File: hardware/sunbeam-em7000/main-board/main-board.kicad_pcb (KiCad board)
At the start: 2 copper layers, 0 parts

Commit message: main-board: placement candidate 1
Co-Authored-By: Claude Sonnet 5.5 <noreply@anthropic.com>
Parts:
- added C101: 100nF_X2, Capacitor_THT:C_Rect_L13.0mm_W6.0mm_P10.00mm_FKS3_FKP3_MKS4, F.Cu at (14.5, 77.0)
- added C201: 100n, Capacitor_SMD:C_0603_1608Metric, F.Cu at (56.0, 109.0)
- added C202: 100n, Capacitor_SMD:C_1206_3216Metric, F.Cu at (59.0, 113.5)
- added C203: 4.7n, Capacitor_SMD:C_0603_1608Metric, F.Cu at (70.8, 112.2)
- added C204: 100n, Capacitor_SMD:C_1206_3216Metric, F.Cu at (62.7, 111.5)
- added C205: 4.7n, Capacitor_SMD:C_0603_1608Metric, F.Cu at (61.6, 106.3)
- added C301: 100 nF, Capacitor_SMD:C_0603_1608Metric, F.Cu at (87.0, 61.2)
- added C302: 47 uF, Capacitor_SMD:CP_Elec_6.3x5.2, F.Cu at (86.0, 67.8)
- added C303: 10 uF, Capacitor_SMD:C_0603_1608Metric, F.Cu at (83.3, 45.4)
- added C304: 22 uF, Capacitor_SMD:C_0805_2012Metric, F.Cu at (86.3, 37.3)
- added C305: 22 uF, Capacitor_SMD:C_0805_2012Metric, F.Cu at (85.2, 35.1)
- added C401: 100 nF, Capacitor_SMD:C_0603_1608Metric, F.Cu at (87.2, 28.9)
- added C402: 100 nF, Capacitor_SMD:C_0603_1608Metric, F.Cu at (102.2, 24.7)
- added C403: 100 nF, Capacitor_SMD:C_0603_1608Metric, F.Cu at (103.0, 11.9)
- added C404: 100 nF, Capacitor_SMD:C_0603_1608Metric, F.Cu at (85.8, 8.05)
- added C405: 100 nF, Capacitor_SMD:C_0603_1608Metric, F.Cu at (82.8, 25.2)
- added C406: 100 nF, Capacitor_SMD:C_0603_1608Metric, F.Cu at (85.5, 28.9)
- added C407: 4.7 uF, Capacitor_SMD:C_0603_1608Metric, F.Cu at (103.0, 10.2)
- added C408: 100 nF, Capacitor_SMD:C_0603_1608Metric, F.Cu at (99.7, 29.1)
- added C409: 1 uF, Capacitor_SMD:C_0603_1608Metric, F.Cu at (101.4, 29.1)
- added C410: 100 nF, Capacitor_SMD:C_0603_1608Metric, F.Cu at (96.3, 29.1)
- added C411: 1 uF, Capacitor_SMD:C_0603_1608Metric, F.Cu at (98.0, 29.1)
- added C412: 2.2 uF, Capacitor_SMD:C_0603_1608Metric, F.Cu at (103.0, 13.6)
- added C413: 2.2 uF, Capacitor_SMD:C_0603_1608Metric, F.Cu at (87.5, 8.05)
- added C414: 20 pF, Capacitor_SMD:C_0603_1608Metric, F.Cu at (89.0, 32.5)
- added C415: 20 pF, Capacitor_SMD:C_0603_1608Metric, F.Cu at (93.3, 34.6)
- added C416: 4.7 pF, Capacitor_SMD:C_0603_1608Metric, F.Cu at (83.8, 28.9)
- added C417: 4.7 pF, Capacitor_SMD:C_0603_1608Metric, F.Cu at (85.8, 31.4)
- added C418: 100 nF, Capacitor_SMD:C_0603_1608Metric, F.Cu at (114.3, 31.8)
- added C419: 4.7 nF, Capacitor_SMD:C_1206_3216Metric, F.Cu at (79.7, 7.65)
- added C422: 100 nF, Capacitor_SMD:C_0603_1608Metric, F.Cu at (101.1, 64.4)
- added C501: 47n, Capacitor_SMD:C_0603_1608Metric, F.Cu at (97.0, 31.5)
- added C502: 47n, Capacitor_SMD:C_0603_1608Metric, F.Cu at (103.8, 28.3)
- added C503: 47n, Capacitor_SMD:C_0603_1608Metric, F.Cu at (108.3, 20.7)
- added C520: 47n, Capacitor_SMD:C_0603_1608Metric, F.Cu at (123.5, 23.7)
- added C521: 100n, Capacitor_SMD:C_0603_1608Metric, F.Cu at (113.8, 17.6)
- added C522: 47n, Capacitor_SMD:C_0603_1608Metric, F.Cu at (105.8, 16.5)
- added C523: 47n, Capacitor_SMD:C_0603_1608Metric, F.Cu at (105.8, 21.6)
- added C524: 47n, Capacitor_SMD:C_0603_1608Metric, F.Cu at (106.3, 29.1)
- added C570: 47n, Capacitor_SMD:C_0603_1608Metric, F.Cu at (105.9, 32.5)
- added C571: 47n, Capacitor_SMD:C_0603_1608Metric, F.Cu at (107.5, 26.6)
- added C601: 4.7n, Capacitor_SMD:C_0805_2012Metric, F.Cu at (54.4, 88.3)
- added C602: 4.7n, Capacitor_SMD:C_0805_2012Metric, F.Cu at (54.4, 86.1)
- added C603: 1u, Capacitor_SMD:C_0603_1608Metric, F.Cu at (53.7, 78.2)
- added C604: 1n, Capacitor_SMD:C_0603_1608Metric, F.Cu at (55.4, 78.3)
- added C605: 100n, Capacitor_SMD:C_0603_1608Metric, F.Cu at (51.5, 83.3)
- added C606: 1n, Capacitor_SMD:C_0603_1608Metric, F.Cu at (52.0, 78.4)
- added C607: 100n, Capacitor_SMD:C_1206_3216Metric, F.Cu at (53.8, 81.2)
- added C608: 1n, Capacitor_SMD:C_0603_1608Metric, F.Cu at (54.6, 83.3)
- added C609: 1n, Capacitor_SMD:C_0603_1608Metric, F.Cu at (70.3, 85.3)
- added C610: 1u, Capacitor_SMD:C_0603_1608Metric, F.Cu at (69.6, 87.8)
- added C611: 100n, Capacitor_SMD:C_0603_1608Metric, F.Cu at (72.5, 91.2)
- added C612: 100n, Capacitor_SMD:C_0603_1608Metric, F.Cu at (69.6, 82.8)
- added C630: 1n, Capacitor_SMD:C_0603_1608Metric, F.Cu at (102.6, 96.5)
- added C640: 10n, Capacitor_SMD:C_0603_1608Metric, F.Cu at (82.7, 106.5)
- added C641: 100n, Capacitor_SMD:C_0603_1608Metric, F.Cu at (79.2, 100.0)
- added C642: 100n, Capacitor_SMD:C_0603_1608Metric, F.Cu at (79.2, 101.7)
- added C645: 10n, Capacitor_SMD:C_0603_1608Metric, F.Cu at (85.3, 116.5)
- added C646: 100n, Capacitor_SMD:C_0603_1608Metric, F.Cu at (80.2, 107.7)
- added C647: 100n, Capacitor_SMD:C_0603_1608Metric, F.Cu at (82.7, 108.5)
- added C670: 100n, Capacitor_SMD:C_0603_1608Metric, F.Cu at (89.3, 108.2)
- added C671: 10u, Capacitor_SMD:C_0805_2012Metric, F.Cu at (89.1, 100.5)
- added C672: 100n, Capacitor_SMD:C_0603_1608Metric, F.Cu at (98.7, 113.2)
- added C673: 100n, Capacitor_SMD:C_0603_1608Metric, F.Cu at (98.7, 100.2)
- added C675: 100n, Capacitor_SMD:C_0603_1608Metric, F.Cu at (89.3, 118.9)
- added C676: 10u, Capacitor_SMD:C_0805_2012Metric, F.Cu at (89.1, 111.7)
- added C677: 100n, Capacitor_SMD:C_0603_1608Metric, F.Cu at (95.1, 122.0)
- added C678: 100n, Capacitor_SMD:C_0603_1608Metric, F.Cu at (98.7, 110.0)
- added C701: 100nF_X2, Capacitor_THT:C_Rect_L13.0mm_W6.0mm_P10.00mm_FKS3_FKP3_MKS4, F.Cu at (41.5, 39.9)
- added C711: 100nF_X2, Capacitor_THT:C_Rect_L13.0mm_W6.0mm_P10.00mm_FKS3_FKP3_MKS4, F.Cu at (41.5, 10.9)
- added C791: 100n, Capacitor_SMD:C_0603_1608Metric, F.Cu at (87.1, 47.2)
- added C792: 47u, Capacitor_SMD:CP_Elec_5x5.4, F.Cu at (92.0, 49.0)
- added C861: 100n, Capacitor_SMD:C_0603_1608Metric, F.Cu at (110.2, 7.55)
- added C862: 100n, Capacitor_SMD:C_0603_1608Metric, F.Cu at (112.8, 8.35)
- added C863: 100n, Capacitor_SMD:C_0603_1608Metric, F.Cu at (122.1, 118.0)
- added D201: BAT54HT1G, Diode_SMD:D_SOD-323, F.Cu at (64.0, 115.2)
- added D202: BAS116, Package_TO_SOT_SMD:SOT-23, F.Cu at (69.2, 115.1)
- added D203: BAT54HT1G, Diode_SMD:D_SOD-323, F.Cu at (65.5, 112.2)
- added D204: BAS116, Package_TO_SOT_SMD:SOT-23, F.Cu at (66.5, 108.5)
- added D205: BAS116, Package_TO_SOT_SMD:SOT-23, F.Cu at (63.2, 97.7)
- added D206: BAS116, Package_TO_SOT_SMD:SOT-23, F.Cu at (66.9, 96.2)
- added D401: USBLC6-2SC6, Package_TO_SOT_SMD:SOT-23-6, F.Cu at (68.8, 8.20)
- added D402: SMF6.0A, Diode_SMD:D_SOD-123F, F.Cu at (82.8, 4.30)
- added D501: PESD5V0F1BL, Diode_SMD:D_SOD-882, F.Cu at (117.2, 39.5)
- added D502: BAT54S, Package_TO_SOT_SMD:SOT-23, F.Cu at (109.5, 17.2)
- added D503: PESD5V0F1BL, Diode_SMD:D_SOD-882, F.Cu at (117.4, 48.0)
- added D504: BAT54S, Package_TO_SOT_SMD:SOT-23, F.Cu at (110.7, 66.2)
- added D505: PESD5V0F1BL, Diode_SMD:D_SOD-882, F.Cu at (122.8, 55.5)
- added D506: BAT54S, Package_TO_SOT_SMD:SOT-23, F.Cu at (110.7, 111.9)
- added D520: PESD5V0F1BL, Diode_SMD:D_SOD-882, F.Cu at (122.9, 20.4)
- added D521: PESD5V0F1BL, Diode_SMD:D_SOD-882, F.Cu at (107.1, 125.8)
- added D522: PESD5V0F1BL, Diode_SMD:D_SOD-882, F.Cu at (109.6, 125.8)
- added D523: BAT54S, Package_TO_SOT_SMD:SOT-23, F.Cu at (102.0, 53.1)
- added D524: BAT54S, Package_TO_SOT_SMD:SOT-23, F.Cu at (101.8, 57.0)
- added D525: PESD5V0F1BL, Diode_SMD:D_SOD-882, F.Cu at (118.7, 120.2)
- added D526: PESD5V0F1BL, Diode_SMD:D_SOD-882, F.Cu at (121.1, 125.8)
- added D527: BAT54S, Package_TO_SOT_SMD:SOT-23, F.Cu at (120.4, 12.8)
- added D528: BAT54S, Package_TO_SOT_SMD:SOT-23, F.Cu at (102.0, 49.2)
- added D529: PESD5V0F1BL, Diode_SMD:D_SOD-882, F.Cu at (109.3, 52.3)
- added D530: PESD5V0F1BL, Diode_SMD:D_SOD-882, F.Cu at (122.8, 70.0)
- added D531: PESD5V0F1BL, Diode_SMD:D_SOD-882, F.Cu at (106.5, 66.6)
- added D570: PESD5V0F1BL, Diode_SMD:D_SOD-882, F.Cu at (113.6, 54.6)
- added D571: PESD5V0F1BL, Diode_SMD:D_SOD-882, F.Cu at (111.0, 54.6)
- added D731: 1N4148WS, Diode_SMD:D_SOD-323, F.Cu at (71.7, 45.6)
- added D741: 1N4148WS, Diode_SMD:D_SOD-323, F.Cu at (69.5, 46.5)
- added D821: 1N4148WS, Diode_SMD:D_SOD-323, F.Cu at (95.0, 42.6)
- added F101: 10A_T_250V, Fuse:Fuseholder_Clip-5x20mm_Bel_FC-203-22_Lateral_P17.80x5.00mm_D1.17mm_Horizontal, F.Cu at (38.0, 93.4)
- added F401: MF-MSMF050-2, Fuse:Fuse_1812_4532Metric, F.Cu at (79.2, 12.0)
- added F520: MF-NSMF012-2, Fuse:Fuse_1206_3216Metric, F.Cu at (103.0, 93.2)
- added F521: MF-NSMF012-2, Fuse:Fuse_1206_3216Metric, F.Cu at (104.4, 118.3)
- added F522: MF-NSMF012-2, Fuse:Fuse_1206_3216Metric, F.Cu at (123.2, 60.0)
- added F523: MF-NSMF012-2, Fuse:Fuse_1206_3216Metric, F.Cu at (109.8, 99.2)
- added F524: MF-NSMF012-2, Fuse:Fuse_1206_3216Metric, F.Cu at (115.5, 87.5)
- added F601: 600R@100MHz, Inductor_SMD:L_0603_1608Metric, F.Cu at (49.5, 77.7)
- added F602: 600R@100MHz, Inductor_SMD:L_0603_1608Metric, F.Cu at (47.8, 86.0)
- added F701: 0.8A, main-board:FUSEHOLDER_5x20_XC_BLX-A, F.Cu at (26.0, 31.4)
- added F711: 0.5A, main-board:FUSEHOLDER_5x20_XC_BLX-A, F.Cu at (26.0, 19.4)
- added F731: 0.4A, main-board:FUSEHOLDER_5x20_XC_BLX-A, F.Cu at (21.5, 66.0)
- added FB301: 600R@100MHz, Inductor_SMD:L_0603_1608Metric, F.Cu at (105.1, 25.9)
- added FID1: Fiducial, Fiducial_1mm_Mask2mm, F.Cu at (14.0, 5.50)
- added FID2: Fiducial, Fiducial_1mm_Mask2mm, F.Cu at (14.0, 123.5)
- added FID3: Fiducial, Fiducial_1mm_Mask2mm, F.Cu at (129.0, 117.6)
- added H1: MountingHole, MountingHole_3.1mm_Lid, F.Cu at (6.50, 122.5)
- added H2: MountingHole, MountingHole_3.1mm_Lid, F.Cu at (126.7, 122.5)
- added H3: MountingHole, MountingHole_3.1mm_Lid, F.Cu at (6.50, 5.50)
- added H4: MountingHole, MountingHole_3.1mm_Lid, F.Cu at (127.0, 5.50)
- added J101: TAB1_LINE1, main-board:Tab_BZXC_BTC-3-PCB634908T, F.Cu at (8.50, 108.5)
- added J102: TAB2_LINE_IN, main-board:Tab_BZXC_BTC-3-PCB634908T, F.Cu at (8.50, 99.7)
- added J103: TAB3_NEUTRAL_IN, main-board:Tab_BZXC_BTC-3-PCB634908T, F.Cu at (8.50, 90.9)
- added J106: TAB6_COFVALVE, main-board:Tab_BZXC_BTC-3-PCB634908T, F.Cu at (8.50, 49.9)
- added J107: TAB7_COFFPUMP, main-board:Tab_BZXC_BTC-3-PCB634908T, F.Cu at (8.50, 37.6)
- added J108: TAB8_STEAMPUMP, main-board:Tab_BZXC_BTC-3-PCB634908T, F.Cu at (8.50, 27.8)
- added J109: TAB9_HOTVALVE, main-board:Tab_BZXC_BTC-3-PCB634908T, F.Cu at (8.50, 19.5)
- added J110: WB_RET, main-board:Tab_BZXC_BTC-3-PCB634908T, F.Cu at (8.50, 82.4)
- added J401: SWD, Connector_PinHeader_1.27mm:PinHeader_2x05_P1.27mm_Vertical_SMD, F.Cu at (119.5, 28.5)
- added J402: USB_PANEL, Connector_PinHeader_2.54mm:PinHeader_1x05_P2.54mm_Vertical, F.Cu at (68.5, 4.50)
- added J501: TEMP_C, Connector_PinHeader_2.54mm:PinHeader_1x02_P2.54mm_Vertical, F.Cu at (120.0, 39.5)
- added J502: TEMP_S, Connector_PinHeader_2.54mm:PinHeader_1x02_P2.54mm_Vertical, F.Cu at (120.0, 47.5)
- added J503: TEMP_W, Connector_PinHeader_2.54mm:PinHeader_1x02_P2.54mm_Vertical, F.Cu at (120.0, 55.5)
- added J520: FLOW, Connector_PinHeader_2.54mm:PinHeader_1x03_P2.54mm_Vertical, F.Cu at (115.0, 20.5)
- added J521: STM_D, Connector_PinHeader_2.54mm:PinHeader_1x04_P2.54mm_Vertical, F.Cu at (102.0, 123.0)
- added J522: BREW_D, Connector_PinHeader_2.54mm:PinHeader_1x04_P2.54mm_Vertical, F.Cu at (113.5, 123.0)
- added J523: SPARE_A, Connector_PinHeader_2.54mm:PinHeader_1x04_P2.54mm_Vertical, F.Cu at (106.5, 44.7)
- added J524: BREW_A, Connector_PinHeader_2.54mm:PinHeader_1x04_P2.54mm_Vertical, F.Cu at (120.0, 62.2)
- added J525: SPARE_AN2_H, Connector_PinHeader_2.54mm:PinHeader_1x04_P2.54mm_Vertical, F.Cu at (106.5, 56.2)
- added J570: CURR1_H, Connector_PinHeader_2.54mm:PinHeader_1x03_P2.54mm_Vertical, F.Cu at (116.0, 57.5)
- added J571: CURR2_H, Connector_PinHeader_2.54mm:PinHeader_1x03_P2.54mm_Vertical, F.Cu at (111.0, 57.5)
- added J620: PT1_H, Connector_JST:JST_XH_B4B-XH-A_1x04_P2.50mm_Vertical, F.Cu at (110.5, 86.2)
- added J622: PT1_2W_P, Connector_PinHeader_2.54mm:PinHeader_1x02_P2.54mm_Vertical, F.Cu at (106.2, 99.2)
- added J623: PT1_23W_N, Connector_PinHeader_2.54mm:PinHeader_1x02_P2.54mm_Vertical, F.Cu at (106.2, 105.7)
- added J625: PT2_H, Connector_JST:JST_XH_B4B-XH-A_1x04_P2.50mm_Vertical, F.Cu at (110.5, 72.2)
- added J627: PT2_2W_P, Connector_PinHeader_2.54mm:PinHeader_1x02_P2.54mm_Vertical, F.Cu at (115.8, 67.2)
- added J628: PT2_23W_N, Connector_PinHeader_2.54mm:PinHeader_1x02_P2.54mm_Vertical, F.Cu at (122.8, 78.7)
- added J630: WT1_H, Connector_JST:JST_PH_B5B-PH-K_1x05_P2.00mm_Vertical, F.Cu at (114.5, 99.5)
- added J635: WT2_H, Connector_JST:JST_PH_B5B-PH-K_1x05_P2.00mm_Vertical, F.Cu at (118.5, 74.5)
- added J761: WB_LV10, Connector_PinHeader_2.54mm:PinHeader_1x10_P2.54mm_Vertical, F.Cu at (130.0, 60.5)
- added J791: SP2, Connector_JST:JST_PH_B9B-PH-K_1x09_P2.00mm_Vertical, F.Cu at (129.0, 12.5)
- added J821: CON2, Connector_JST:JST_PH_B9B-PH-K_1x09_P2.00mm_Vertical, F.Cu at (129.0, 34.5)
- added J861: KNOB, Connector_JST:JST_PH_B4B-PH-K_1x04_P2.00mm_Vertical, F.Cu at (110.0, 11.5)
- added J862: REED, main-board:REED_PADS_P20.00mm, F.Cu at (122.0, 91.5)
- added JP101: LINK_LIVE, main-board:JP101_WireLink_P10mm, F.Cu at (34.0, 84.5)
- added JP301: SEL_5V, Connector_PinHeader_2.54mm:PinHeader_1x03_P2.54mm_Vertical, F.Cu at (90.0, 54.5)
- added JP302: LINK_3V3, Connector_PinHeader_2.54mm:PinHeader_1x02_P2.54mm_Vertical, F.Cu at (73.5, 35.7)
- added JP303: LINK_MOD, main-board:JP101_WireLink_P10mm, F.Cu at (26.5, 50.5)
- added JP401: BOOT0_HI, Connector_PinHeader_2.54mm:PinHeader_1x02_P2.54mm_Vertical, F.Cu at (66.2, 15.0)
- added JP402: LINK_VTREF, Connector_PinHeader_2.54mm:PinHeader_1x02_P2.54mm_Vertical, F.Cu at (66.2, 21.0)
- added JP761: LINK, Connector_PinHeader_2.54mm:PinHeader_1x02_P2.54mm_Vertical, F.Cu at (127.3, 55.9)
- added JP791: LINK, Connector_PinHeader_2.54mm:PinHeader_1x02_P2.54mm_Vertical, F.Cu at (98.0, 50.7)
- added JP821: LINK, Connector_PinHeader_2.54mm:PinHeader_1x02_P2.54mm_Vertical, F.Cu at (98.0, 57.2)
- added K201: HF115F-Q/005-1H, main-board:Relay_HF115F-Q_1H_Vertical, F.Cu at (55.5, 105.7)
- added K731: HF32FA-G/005-HSL1, main-board:RELAY_HF32FA-G_1H_TYPE1_THT, F.Cu at (60.7, 46.5)
- added K741: HF32FA-G/005-HSL1, main-board:RELAY_HF32FA-G_1H_TYPE1_THT, F.Cu at (60.7, 11.3)
- added Q201: NX3008NBK, Package_TO_SOT_SMD:SOT-23, F.Cu at (71.0, 107.6)
- added Q202: NX3008NBK, Package_TO_SOT_SMD:SOT-23, F.Cu at (67.3, 104.4)
- added Q701: AO3400A, Package_TO_SOT_SMD:SOT-23, F.Cu at (62.0, 25.8)
- added Q711: AO3400A, Package_TO_SOT_SMD:SOT-23, F.Cu at (64.5, 43.0)
- added Q731: AO3400A, Package_TO_SOT_SMD:SOT-23, F.Cu at (69.8, 35.5)
- added Q741: AO3400A, Package_TO_SOT_SMD:SOT-23, F.Cu at (68.5, 43.0)
- added Q761: AO3400A, Package_TO_SOT_SMD:SOT-23, F.Cu at (97.0, 76.3)
- added Q771: AO3400A, Package_TO_SOT_SMD:SOT-23, F.Cu at (94.0, 59.2)
- added Q821: AO3400A, Package_TO_SOT_SMD:SOT-23, F.Cu at (97.7, 69.5)
- added Q822: AO3401A, Package_TO_SOT_SMD:SOT-23, F.Cu at (98.0, 63.7)
- added Q823: AO3400A, Package_TO_SOT_SMD:SOT-23, F.Cu at (80.5, 45.5)
- added Q824: AO3400A, Package_TO_SOT_SMD:SOT-23, F.Cu at (73.5, 42.0)
- added R101: 1Meg, Resistor_SMD:R_1206_3216Metric, F.Cu at (26.4, 67.4)
- added R102: 1Meg, Resistor_SMD:R_1206_3216Metric, F.Cu at (27.9, 63.8)
- added R103: 1Meg, Resistor_SMD:R_1206_3216Metric, F.Cu at (19.1, 69.6)
- added R104: 1Meg, Resistor_SMD:R_1206_3216Metric, F.Cu at (19.1, 74.4)
- added R105: 1m, main-board:R_WSK2512_4T, F.Cu at (9.00, 86.7)
- added R201: 100k, Resistor_SMD:R_0603_1608Metric, F.Cu at (51.0, 112.2)
- added R202: 100k, Resistor_SMD:R_0603_1608Metric, F.Cu at (51.0, 110.5)
- added R203: 5.6Meg, Resistor_SMD:R_0603_1608Metric, F.Cu at (70.8, 110.5)
- added R204: 5.6Meg, Resistor_SMD:R_0603_1608Metric, F.Cu at (63.5, 104.6)
- added R205: 100k, Resistor_SMD:R_0603_1608Metric, F.Cu at (66.5, 116.0)
- added R206: 100k, Resistor_SMD:R_0603_1608Metric, F.Cu at (63.1, 108.2)
- added R207: 1k, Resistor_SMD:R_0603_1608Metric, F.Cu at (53.5, 110.1)
- added R301: 0, Resistor_SMD:R_0603_1608Metric, F.Cu at (117.2, 35.5)
- added R302: 0, Resistor_SMD:R_0603_1608Metric, F.Cu at (110.0, 20.7)
- added R401: 10k, Resistor_SMD:R_0603_1608Metric, F.Cu at (69.7, 12.2)
- added R402: 1k, Resistor_SMD:R_0603_1608Metric, F.Cu at (117.0, 23.9)
- added R403: 1Meg, Resistor_SMD:R_1206_3216Metric, F.Cu at (65.3, 5.75)
- added R501: 10k, Resistor_SMD:R_0603_1608Metric, F.Cu at (119.7, 36.8)
- added R502: 1k, Resistor_SMD:R_0603_1608Metric, F.Cu at (100.2, 31.5)
- added R503: 10k, Resistor_SMD:R_0603_1608Metric, F.Cu at (115.8, 48.0)
- added R504: 1k, Resistor_SMD:R_0603_1608Metric, F.Cu at (103.5, 31.7)
- added R505: 10k, Resistor_SMD:R_0603_1608Metric, F.Cu at (116.3, 50.5)
- added R506: 1k, Resistor_SMD:R_0603_1608Metric, F.Cu at (105.8, 19.9)
- added R520: 10k, Resistor_SMD:R_0603_1608Metric, F.Cu at (113.8, 23.3)
- added R521: 1k, Resistor_SMD:R_0603_1608Metric, F.Cu at (123.5, 22.0)
- added R522: 0, Resistor_SMD:R_0603_1608Metric, F.Cu at (95.0, 7.10)
- added R523: 100, Resistor_SMD:R_0603_1608Metric, F.Cu at (82.0, 22.6)
- added R524: 100, Resistor_SMD:R_0603_1608Metric, F.Cu at (81.1, 25.1)
- added R525: 2.2k, Resistor_SMD:R_0603_1608Metric, F.Cu at (69.7, 18.2)
- added R526: 2.2k, Resistor_SMD:R_0603_1608Metric, F.Cu at (66.5, 23.8)
- added R527: 100, Resistor_SMD:R_0603_1608Metric, F.Cu at (102.2, 16.1)
- added R528: 100, Resistor_SMD:R_0603_1608Metric, F.Cu at (105.4, 13.4)
- added R529: 2.2k, Resistor_SMD:R_0603_1608Metric, F.Cu at (113.5, 15.8)
- added R530: 2.2k, Resistor_SMD:R_0603_1608Metric, F.Cu at (105.4, 10.2)
- added R531: 10k, Resistor_SMD:R_0603_1608Metric, F.Cu at (110.0, 44.0)
- added R532: 20k, Resistor_SMD:R_0603_1608Metric, F.Cu at (105.9, 41.2)
- added R533: 1k, Resistor_SMD:R_0603_1608Metric, F.Cu at (105.8, 18.2)
- added R534: 10k, Resistor_SMD:R_0603_1608Metric, F.Cu at (124.6, 56.0)
- added R535: 20k, Resistor_SMD:R_0603_1608Metric, F.Cu at (124.3, 48.0)
- added R536: 1k, Resistor_SMD:R_0603_1608Metric, F.Cu at (105.8, 23.3)
- added R537: 10k, Resistor_SMD:R_0603_1608Metric, F.Cu at (111.0, 52.1)
- added R538: 20k, Resistor_SMD:R_0603_1608Metric, F.Cu at (110.2, 49.6)
- added R539: 1k, Resistor_SMD:R_0603_1608Metric, F.Cu at (103.8, 30.0)
- added R540: 0, Resistor_SMD:R_1206_3216Metric, F.Cu at (101.9, 111.8)
- added R541: 0, Resistor_SMD:R_1206_3216Metric, F.Cu at (112.6, 119.8)
- added R542: 0, Resistor_SMD:R_1206_3216Metric, F.Cu at (123.2, 52.0)
- added R543: 0, Resistor_SMD:R_1206_3216Metric, F.Cu at (114.8, 92.2)
- added R544: 0, Resistor_SMD:R_1206_3216Metric, F.Cu at (123.2, 66.8)
- added R570: 10k, Resistor_SMD:R_0603_1608Metric, F.Cu at (113.5, 50.5)
- added R571: 20k, Resistor_SMD:R_0603_1608Metric, F.Cu at (114.2, 46.5)
- added R572: DNP, Resistor_SMD:R_0603_1608Metric, F.Cu at (114.0, 43.4)
- added R573: 1k, Resistor_SMD:R_0603_1608Metric, F.Cu at (105.1, 35.6)
- added R574: 10k, Resistor_SMD:R_0603_1608Metric, F.Cu at (122.8, 41.8)
- added R575: 20k, Resistor_SMD:R_0603_1608Metric, F.Cu at (122.8, 36.9)
- added R576: DNP, Resistor_SMD:R_0603_1608Metric, F.Cu at (123.5, 39.4)
- added R577: 1k, Resistor_SMD:R_0603_1608Metric, F.Cu at (108.8, 28.3)
- added R601: 300k, Resistor_SMD:R_2512_6332Metric, F.Cu at (24.9, 72.6)
- added R602: 300k, Resistor_SMD:R_2512_6332Metric, F.Cu at (27.4, 78.6)
- added R603: 300k, Resistor_SMD:R_2512_6332Metric, F.Cu at (35.4, 80.3)
- added R604: 750, Resistor_SMD:R_0603_1608Metric, F.Cu at (45.5, 90.2)
- added R605: 49.9, Resistor_SMD:R_0603_1608Metric, F.Cu at (48.0, 89.5)
- added R606: 49.9, Resistor_SMD:R_0603_1608Metric, F.Cu at (48.0, 91.2)
- added R607: 330, Resistor_SMD:R_0603_1608Metric, F.Cu at (48.4, 87.8)
- added R608: 330, Resistor_SMD:R_0603_1608Metric, F.Cu at (51.0, 86.0)
- added R609: 33, Resistor_SMD:R_0603_1608Metric, F.Cu at (71.4, 82.9)
- added R610: 33, Resistor_SMD:R_0603_1608Metric, F.Cu at (101.4, 8.45)
- added R611: 33, Resistor_SMD:R_0603_1608Metric, F.Cu at (98.1, 8.80)
- added R612: 33, Resistor_SMD:R_0603_1608Metric, F.Cu at (98.2, 7.10)
- added R613: 33, Resistor_SMD:R_0603_1608Metric, F.Cu at (68.5, 90.5)
- added R614: 100k, Resistor_SMD:R_0603_1608Metric, F.Cu at (65.2, 90.5)
- added R615: 100k, Resistor_SMD:R_0603_1608Metric, F.Cu at (115.5, 35.6)
- added R630: 60.4k, Resistor_SMD:R_2512_6332Metric, F.Cu at (40.6, 121.8)
- added R631: 60.4k, Resistor_SMD:R_2512_6332Metric, F.Cu at (48.5, 122.7)
- added R632: 22k, Resistor_SMD:R_0603_1608Metric, F.Cu at (101.7, 104.0)
- added R640: 4.02k, Resistor_SMD:R_0603_1608Metric, F.Cu at (105.7, 86.1)
- added R641: 100k, Resistor_SMD:R_0603_1608Metric, F.Cu at (105.2, 89.3)
- added R642: 0, Resistor_SMD:R_0603_1608Metric, F.Cu at (79.5, 119.3)
- added R643: 0, Resistor_SMD:R_0603_1608Metric, F.Cu at (80.0, 104.2)
- added R645: 4.02k, Resistor_SMD:R_0603_1608Metric, F.Cu at (81.3, 120.8)
- added R646: 100k, Resistor_SMD:R_0603_1608Metric, F.Cu at (105.2, 92.5)
- added R647: 0, Resistor_SMD:R_0603_1608Metric, F.Cu at (83.8, 124.8)
- added R648: 0, Resistor_SMD:R_0603_1608Metric, F.Cu at (81.3, 124.0)
- added R670: 100, Resistor_SMD:R_0603_1608Metric, F.Cu at (98.7, 106.8)
- added R671: 100, Resistor_SMD:R_0603_1608Metric, F.Cu at (89.3, 105.0)
- added R672: 100k, Resistor_SMD:R_0603_1608Metric, F.Cu at (105.2, 95.8)
- added R675: 100, Resistor_SMD:R_0603_1608Metric, F.Cu at (89.2, 121.3)
- added R676: 100, Resistor_SMD:R_0603_1608Metric, F.Cu at (89.3, 115.7)
- added R677: 100k, Resistor_SMD:R_0603_1608Metric, F.Cu at (105.8, 115.6)
- added R690: 0, Resistor_SMD:R_0603_1608Metric, F.Cu at (105.2, 111.8)
- added R691: 0, Resistor_SMD:R_0603_1608Metric, F.Cu at (105.5, 82.9)
- added R701: 100, Resistor_SMD:R_0603_1608Metric, F.Cu at (89.2, 8.05)
- added R702: 100k, Resistor_SMD:R_0603_1608Metric, F.Cu at (69.0, 39.2)
- added R703: 180, Resistor_SMD:R_1206_3216Metric, F.Cu at (66.0, 46.0)
- added R704: 200, Resistor_SMD:R_1206_3216Metric, F.Cu at (45.0, 26.6)
- added R705: 200, Resistor_SMD:R_1206_3216Metric, F.Cu at (49.9, 26.6)
- added R706: 100, Resistor_SMD:R_2512_6332Metric, F.Cu at (34.8, 28.0)
- added R711: 100, Resistor_SMD:R_0603_1608Metric, F.Cu at (91.7, 7.10)
- added R712: 100k, Resistor_SMD:R_0603_1608Metric, F.Cu at (59.1, 26.0)
- added R713: 180, Resistor_SMD:R_1206_3216Metric, F.Cu at (77.8, 34.7)
- added R714: 200, Resistor_SMD:R_1206_3216Metric, F.Cu at (47.1, 14.5)
- added R715: 200, Resistor_SMD:R_1206_3216Metric, F.Cu at (52.0, 14.3)
- added R716: 100, Resistor_SMD:R_2512_6332Metric, F.Cu at (34.8, 22.7)
- added R731: 100, Resistor_SMD:R_0603_1608Metric, F.Cu at (81.1, 17.9)
- added R732: 100k, Resistor_SMD:R_0603_1608Metric, F.Cu at (83.3, 74.2)
- added R741: 100, Resistor_SMD:R_0603_1608Metric, F.Cu at (79.4, 18.0)
- added R742: 100k, Resistor_SMD:R_0603_1608Metric, F.Cu at (61.6, 36.5)
- added R761: 100, Resistor_SMD:R_0603_1608Metric, F.Cu at (82.8, 13.7)
- added R762: 100k, Resistor_SMD:R_0603_1608Metric, F.Cu at (93.6, 77.2)
- added R763: 180, Resistor_SMD:R_1206_3216Metric, F.Cu at (97.7, 73.0)
- added R764: 27k, Resistor_SMD:R_0603_1608Metric, F.Cu at (102.2, 19.2)
- added R765: 82k, Resistor_SMD:R_0603_1608Metric, F.Cu at (118.5, 7.55)
- added R771: 100, Resistor_SMD:R_0603_1608Metric, F.Cu at (82.8, 16.9)
- added R772: 100k, Resistor_SMD:R_0603_1608Metric, F.Cu at (95.6, 45.1)
- added R773: 180, Resistor_SMD:R_1206_3216Metric, F.Cu at (126.8, 64.0)
- added R774: 27k, Resistor_SMD:R_0603_1608Metric, F.Cu at (82.8, 20.1)
- added R775: 82k, Resistor_SMD:R_0603_1608Metric, F.Cu at (66.5, 18.2)
- added R791: 100, Resistor_SMD:R_0603_1608Metric, F.Cu at (84.7, 47.8)
- added R792: 100, Resistor_SMD:R_0603_1608Metric, F.Cu at (86.3, 49.8)
- added R793: 100, Resistor_SMD:R_0603_1608Metric, F.Cu at (85.2, 45.4)
- added R794: 100, Resistor_SMD:R_0603_1608Metric, F.Cu at (81.8, 35.4)
- added R795: 100, Resistor_SMD:R_0603_1608Metric, F.Cu at (92.4, 37.5)
- added R796: 1k, Resistor_SMD:R_0603_1608Metric, F.Cu at (80.3, 20.4)
- added R797: 1k, Resistor_SMD:R_0603_1608Metric, F.Cu at (94.9, 8.80)
- added R798: 1k, Resistor_SMD:R_0603_1608Metric, F.Cu at (84.2, 8.05)
- added R799: 1k, Resistor_SMD:R_0603_1608Metric, F.Cu at (91.7, 8.80)
- added R800: 1k, Resistor_SMD:R_0603_1608Metric, F.Cu at (75.7, 7.95)
- added R801: 10k, Resistor_SMD:R_0603_1608Metric, F.Cu at (93.7, 56.5)
- added R802: 10k, Resistor_SMD:R_0603_1608Metric, F.Cu at (90.8, 63.0)
- added R803: 10k, Resistor_SMD:R_0603_1608Metric, F.Cu at (87.2, 55.4)
- added R804: 10k, Resistor_SMD:R_0603_1608Metric, F.Cu at (87.1, 52.2)
- added R805: 10k, Resistor_SMD:R_0603_1608Metric, F.Cu at (76.8, 44.8)
- added R806: 10k, Resistor_SMD:R_0603_1608Metric, F.Cu at (83.8, 50.2)
- added R821: 100, Resistor_SMD:R_0603_1608Metric, F.Cu at (79.4, 22.9)
- added R822: 100k, Resistor_SMD:R_0603_1608Metric, F.Cu at (94.2, 70.5)
- added R823: 22k, Resistor_SMD:R_0603_1608Metric, F.Cu at (94.2, 68.6)
- added R824: 22k, Resistor_SMD:R_0603_1608Metric, F.Cu at (98.3, 66.6)
- added R825: 22k, Resistor_SMD:R_0603_1608Metric, F.Cu at (127.2, 59.4)
- added R826: 100, Resistor_SMD:R_0603_1608Metric, F.Cu at (80.0, 29.3)
- added R827: 100k, Resistor_SMD:R_0603_1608Metric, F.Cu at (62.5, 14.8)
- added R828: 100, Resistor_SMD:R_1206_3216Metric, F.Cu at (93.3, 66.5)
- added R829: 100, Resistor_SMD:R_0603_1608Metric, F.Cu at (79.4, 26.1)
- added R830: 100k, Resistor_SMD:R_0603_1608Metric, F.Cu at (74.2, 45.5)
- added R831: 10k, Resistor_SMD:R_0603_1608Metric, F.Cu at (79.3, 31.8)
- added R832: 10k, Resistor_SMD:R_0603_1608Metric, F.Cu at (69.7, 24.8)
- added R833: 10k, Resistor_SMD:R_0603_1608Metric, F.Cu at (82.0, 28.6)
- added R834: 10k, Resistor_SMD:R_0603_1608Metric, F.Cu at (82.6, 31.4)
- added R835: 10k, Resistor_SMD:R_0603_1608Metric, F.Cu at (69.7, 26.5)
- added R861: 10k, Resistor_SMD:R_0603_1608Metric, F.Cu at (108.5, 7.55)
- added R862: 10k, Resistor_SMD:R_0603_1608Metric, F.Cu at (116.0, 8.35)
- added R863: 10k, Resistor_SMD:R_0603_1608Metric, F.Cu at (119.6, 117.3)
- added RT301: NTC 10D-9, Capacitor_THT:C_Disc_D11.0mm_W5.0mm_P7.50mm, F.Cu at (15.3, 45.3)
- added RV101: 14D471K, Varistor:RV_Disc_D15.5mm_W5mm_P7.5mm, F.Cu at (19.5, 82.4)
- added SW401: RESET, main-board:TS1187A_5.1x5.1mm_SMD, F.Cu at (68.5, 30.5)
- added T701: BTA204S-600B, Package_TO_SOT_SMD:TO-252-3_TabPin2, F.Cu at (43.6, 31.4)
- added T711: BTA204S-600B, Package_TO_SOT_SMD:TO-252-3_TabPin2, F.Cu at (43.6, 19.4)
- added TP101: TP_LINE_IN, TestPoint:TestPoint_Pad_D1.5mm, B.Cu at (8.50, 103.8)
- added TP102: TP_LINE_F, TestPoint:TestPoint_Pad_D1.5mm, B.Cu at (13.0, 95.0)
- added TP103: TP_LINE, TestPoint:TestPoint_Pad_D1.5mm, B.Cu at (35.0, 121.8)
- added TP104: TP_LINE1, TestPoint:TestPoint_Pad_D1.5mm, B.Cu at (13.3, 104.2)
- added TP105: TP_NEUTRAL_IN, TestPoint:TestPoint_Pad_D1.5mm, B.Cu at (6.00, 95.0)
- added TP106: TP_NEUTRAL, TestPoint:TestPoint_Pad_D1.5mm, B.Cu at (25.5, 59.5)
- added TP107: TP_NEUTRAL_IN_V, TestPoint:TestPoint_Pad_D1.5mm, B.Cu at (9.00, 95.0)
- added TP108: TP_NEUTRAL_V, TestPoint:TestPoint_Pad_D1.5mm, B.Cu at (26.5, 57.0)
- added TP201: TP_POL_GATE_A, TestPoint:TestPoint_Pad_D1.5mm, B.Cu at (71.0, 103.8)
- added TP202: TP_POL_GATE_B, TestPoint:TestPoint_Pad_D1.5mm, B.Cu at (71.0, 101.0)
- added TP203: TP_POL_OUT, TestPoint:TestPoint_Pad_D1.5mm, B.Cu at (104.5, 3.95)
- added TP204: TP_POL_BUF, TestPoint:TestPoint_Pad_D1.5mm, B.Cu at (54.8, 114.0)
- added TP205: TP_POL_COIL_LO, TestPoint:TestPoint_Pad_D1.5mm, B.Cu at (59.0, 98.5)
- added TP206: TP_+5V, TestPoint:TestPoint_Pad_D1.5mm, B.Cu at (59.5, 110.5)
- added TP301: TP, TestPoint:TestPoint_Pad_D1.5mm, B.Cu at (86.0, 74.5)
- added TP302: TP, TestPoint:TestPoint_Pad_D1.5mm, B.Cu at (66.5, 39.5)
- added TP303: TP, TestPoint:TestPoint_Pad_D1.5mm, B.Cu at (84.5, 54.0)
- added TP401: TP, TestPoint:TestPoint_Pad_D1.5mm, B.Cu at (107.0, 3.95)
- added TP402: TP, TestPoint:TestPoint_Pad_D1.5mm, B.Cu at (108.5, 34.0)
- added TP403: TP, TestPoint:TestPoint_Pad_D1.5mm, B.Cu at (112.0, 4.00)
- added TP404: TP, TestPoint:TestPoint_Pad_D1.5mm, B.Cu at (65.5, 35.0)
- added TP405: TP, TestPoint:TestPoint_Pad_D1.5mm, B.Cu at (120.5, 16.5)
- added TP406: TP, TestPoint:TestPoint_Pad_D1.5mm, B.Cu at (95.8, 37.2)
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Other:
- board outline added: 131 x 125 mm
- copper layers 2 -> 4

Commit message: main-board: placement candidate 2
Co-Authored-By: Claude Sonnet 5.5 <noreply@anthropic.com>
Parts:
- moved R632 83.8 mm to (68.8, 26.9), turned to 0 degrees
- moved C630 79.1 mm to (66.3, 26.1), turned to 90 degrees
- moved D506 76.4 mm to (116.8, 35.8)
- moved R615 54.7 mm to (105.1, 89.3)
- moved R403 54.7 mm to (120.0, 6.95), turned to 0 degrees
- moved D502 49.0 mm to (110.7, 66.2)
- moved D504 45.7 mm to (110.2, 111.9)
- moved R827 41.1 mm to (83.2, 50.2), turned to -90 degrees
- moved TP409 41.0 mm to (113.3, 28.3)
- moved TP530 39.4 mm to (123.0, 73.5)
- moved R835 37.9 mm to (102.0, 46.3), turned to -90 degrees
- moved TP403 37.8 mm to (102.0, 40.5)
- moved R702 37.8 mm to (83.2, 74.2)
- moved TP603 37.3 mm to (24.5, 62.0)
- moved TP408 35.2 mm to (87.0, 3.95)
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
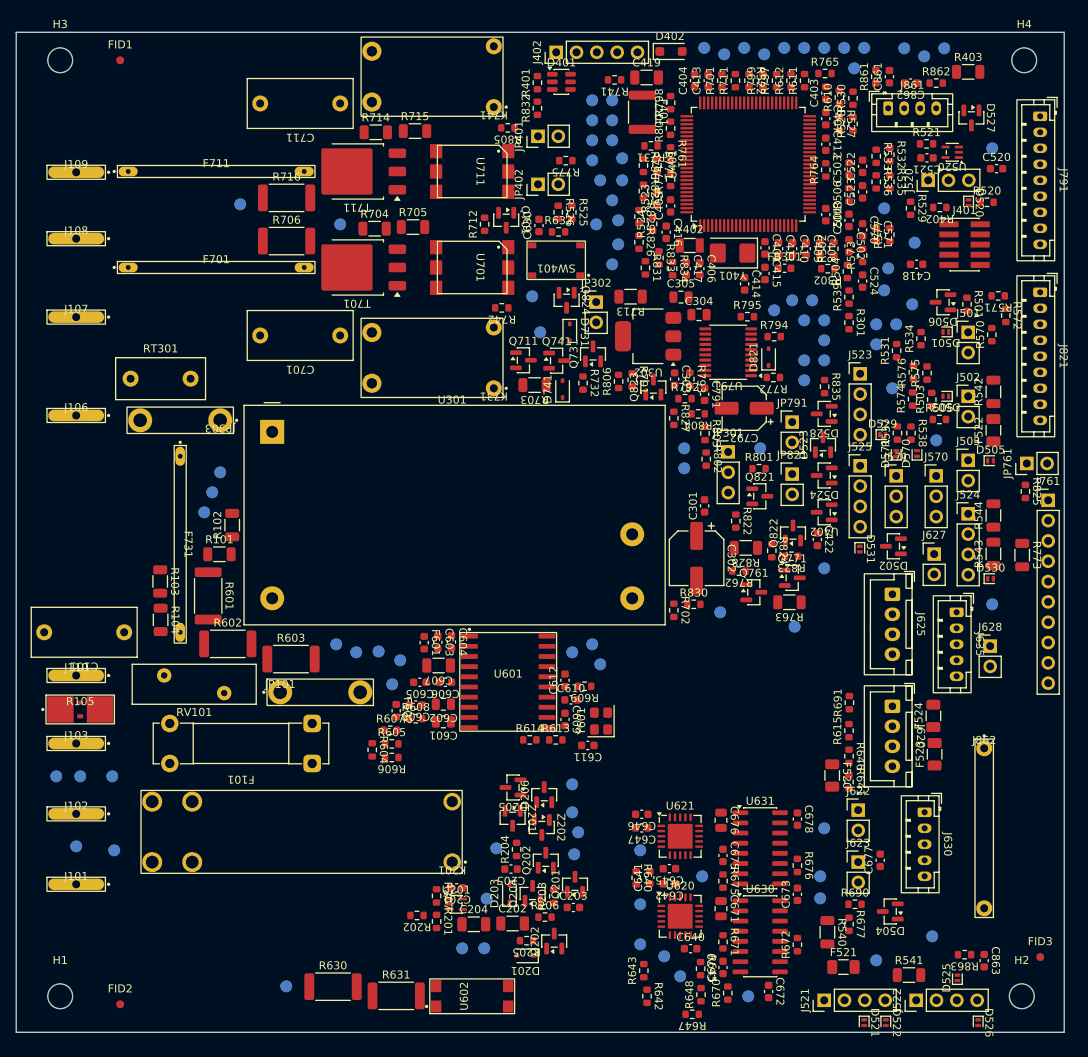
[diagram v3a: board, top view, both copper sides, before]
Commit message: main-board: clear the scriptable hygiene findings (library footprints, silk text, designators, small test points, pin-1 marks, mains entry class) [SOL-HW-MAIN-BOARD-PROVEN-AND-LAID-OUT.C7, .C8]
Co-Authored-By: Claude Sonnet 5.5 <noreply@anthropic.com>
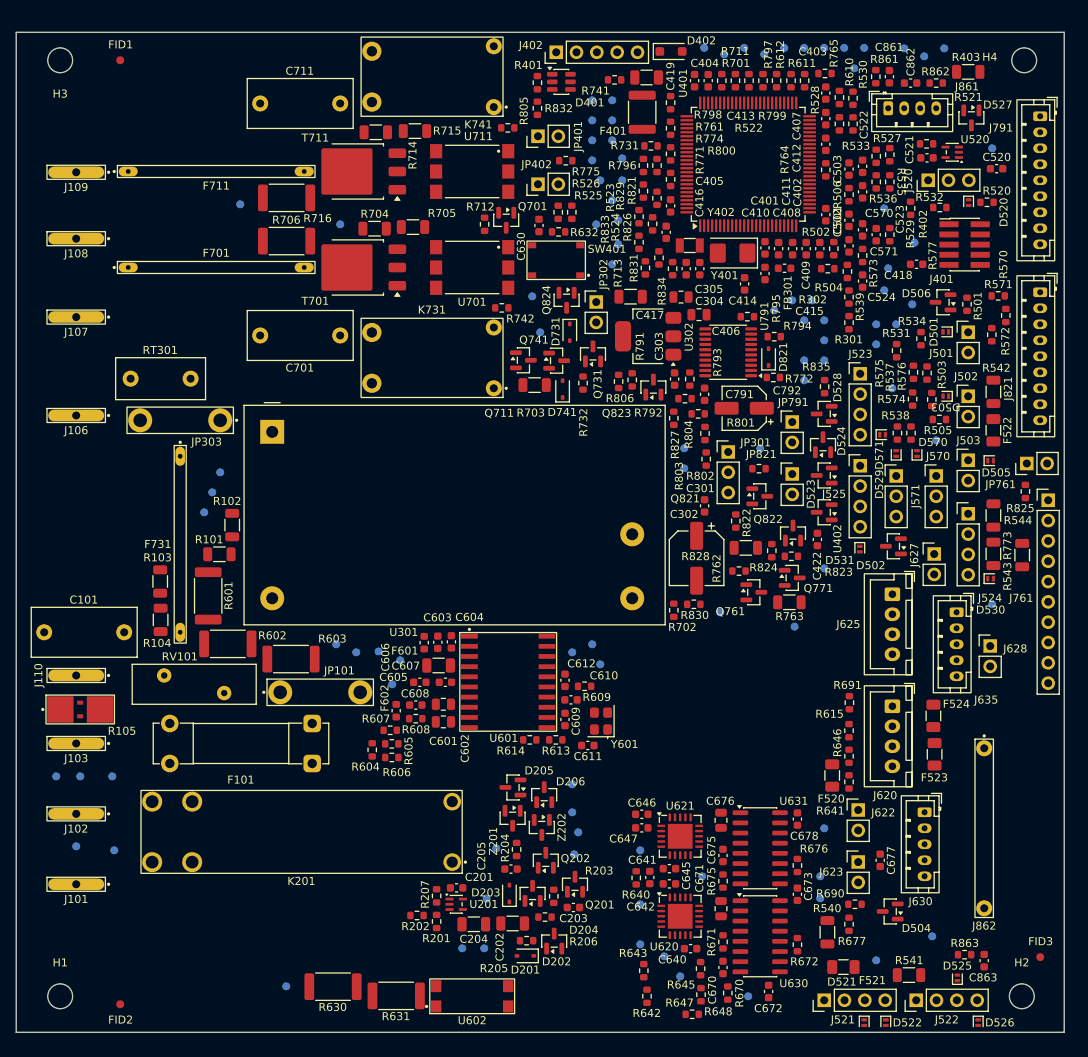
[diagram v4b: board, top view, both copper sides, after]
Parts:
- FID1, FID2, FID3: footprint Fiducial_1mm_Mask2mm -> Fiducial:Fiducial_1mm_Mask2mm
- H1, H2, H3, H4: footprint MountingHole_3.1mm_Lid -> main-board:MountingHole_3.1mm_Lid
- TP101, TP102, TP103, TP104, TP105, TP106, TP107, TP108, TP201, TP202, TP203, TP204, TP205, TP206, TP301, TP302, TP303, TP401, TP402, TP403, TP404, TP405, TP406, TP407, TP408, TP409, TP410, TP411, TP412, TP413, TP501, TP502, TP503, TP520, TP521, TP522, TP523, TP524, TP525, TP526, TP527, TP528, TP529, TP530, TP531, TP532, TP570, TP571, TP601, TP602, TP603, TP604, TP605, TP606, TP607, TP608, TP609, TP610, TP620, TP621, TP622, TP623, TP630, TP670, TP671, TP672, TP673, TP690, TP691, TP701, TP702, TP711, TP712, TP731, TP741, TP761, TP762, TP772, TP791, TP792, TP793, TP794, TP795, TP796, TP821, TP822, TP823, TP824, TP831, TP832, TP833, TP834, TP835, TP861, TP862, TP863: footprint TestPoint:TestPoint_Pad_D1.5mm -> main-board:TestPoint_Pad_D1.0mm_Tight
- Y601: footprint Oscillator:Oscillator_SMD_Abracon_ASE-4Pin_3.2x2.5mm -> main-board:Oscillator_SMD_Abracon_ASE-4Pin_3.2x2.5mm_Pin1Mark

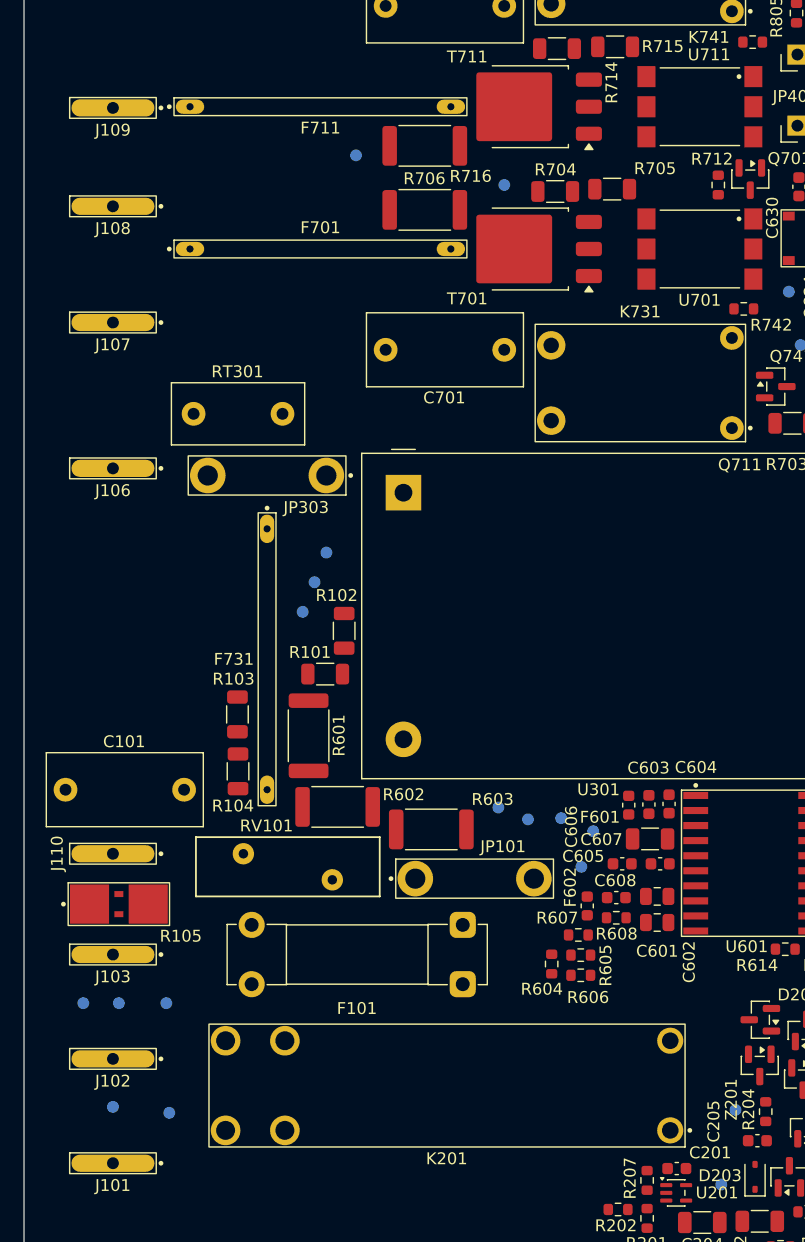
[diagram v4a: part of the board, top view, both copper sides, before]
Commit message: main-board: placement candidate 4
Sixteen parts moved from candidate 2, with Konnect's set_component_placements on the closed board, so that
every mains tab takes an insulated push-on receptacle (2.0 mm hand clearance to parts over 9 mm tall, tab
pitch at least 8.5 mm) and the mains trunk routes at the pollution degree 2 figures: K201 +3.5 mm in x;
F101 to (22, 85) at 0; JP101 to (38.5, 93.9) at 180; C101 up 3.4 mm; RV101 to (15.5, 66) at 180;
RT301 +2.3 mm in x; F711 to (27.7, 24.5); F701 to (27.7, 36.5); J109 up 0.2 mm; R706 and R716 turned
180; C701 to (41, 41.6); TP101, TP104, TP702 and TP712 moved clear of the moved parts. No region bound
or region part list changes. Candidate 3 was a scratch trial and is not committed.

[SOL-HW-MAIN-BOARD-PROVEN-AND-LAID-OUT.C7]

Co-Authored-By: Claude Sonnet 5.5 <noreply@anthropic.com>
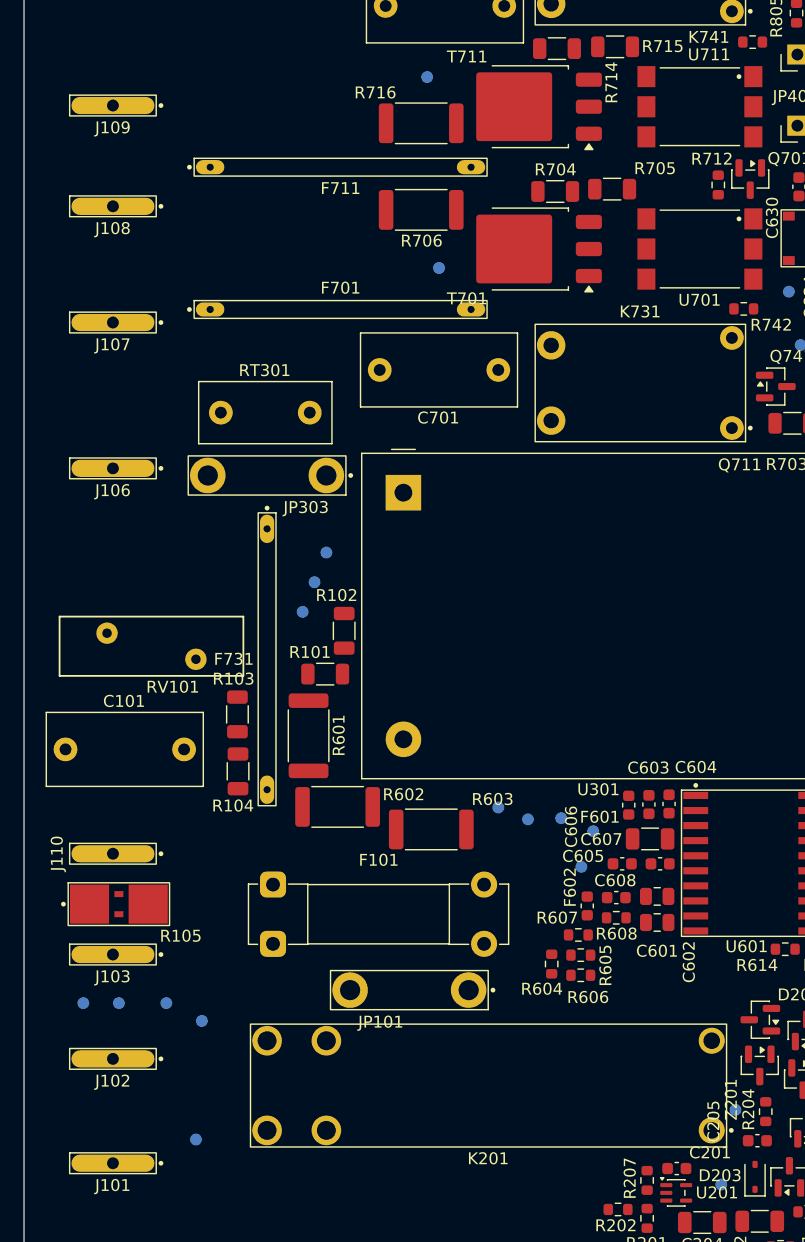
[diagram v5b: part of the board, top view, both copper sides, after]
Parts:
- moved F101 18.1 mm to (22.0, 85.0), turned to 0 degrees
- moved RV101 16.9 mm to (15.5, 66.0), turned to 180 degrees
- moved TP101 10.4 mm to (16.0, 96.5)
- moved JP101 10.4 mm to (38.5, 93.9), turned to 180 degrees
- moved TP712 8.92 mm to (35.0, 16.9)
- moved TP702 8.90 mm to (36.0, 33.0)
- moved F701 5.38 mm to (27.7, 36.5)
- moved F711 5.38 mm to (27.7, 24.5)
- moved K201 3.50 mm to (59.0, 105.7)
- moved C101 3.40 mm to (14.5, 73.6)
- moved TP104 3.18 mm to (15.5, 106.5)
- moved RT301 2.30 mm to (17.6, 45.2)
- moved R716 1.92 mm to (34.5, 20.8), turned to 180 degrees
- moved C701 1.77 mm to (41.0, 41.6)
- moved R706 0.30 mm to (34.5, 28.1), turned to 180 degrees
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
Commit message: main-board: placement candidate 5
Candidate 4 with the test pad TP202 (/Interlock/POL_GATE_B, B.Cu) moved from (61.0, 104.0) to (71.5, 113.75).
Candidate 4's +3.5 mm move of K201 put K201's courtyard over TP202 (0.0 mm, where TEST-5 asks 1 mm). The
new place is the nearest inside `low voltage` that is 1 mm from every courtyard, 2.5 mm from every other
test pad and over 10.5 mm from every mains pad (19.5 mm); it is 7.8 mm from the nearest pad of its net.

[SOL-HW-MAIN-BOARD-PROVEN-AND-LAID-OUT.C7]

Co-Authored-By: Claude Sonnet 5.5 <noreply@anthropic.com>
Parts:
- moved TP202 14.3 mm to (71.5, 113.8)
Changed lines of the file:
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@@
 	(footprint "main-board:TestPoint_Pad_D1.0mm_Tight"
 		(layer "B.Cu")
-		(at 61.0013 104 180)
+		(at 71.5 113.75 180)
 		(descr "SMD pad as test point, diameter 1.0 mm, courtyard 0.25 mm beyond the copper so test points can stand 2.5 mm apart and still keep the 1 mm test-point-to-courtyard distance")
 		(tags "test point SMD pad")
 		(property "Reference" "TP202"
-			(at 0.05 -1.45 0)
+			(at 0.05 -1.45)
 			(unlocked yes)
 			(layer "B.SilkS")
@@
 		)
 		(property "Value" "TP_POL_GATE_B"
-			(at 0 -1.75 0)
+			(at 0 -1.75)
 			(unlocked yes)
 			(layer "B.SilkS")
@@
 		)
 		(property "Datasheet" ""
-			(at 0 0 0)
+			(at 0 0)
 			(layer "B.Fab")
 			(hide yes)
@@
 		)
 		(property "Description" "test point"
-			(at 0 0 0)
+			(at 0 0)
 			(layer "B.Fab")
 			(hide yes)
